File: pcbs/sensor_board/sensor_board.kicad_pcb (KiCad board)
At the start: 2 copper layers, 32 x 51 mm, 45 parts, among them J1 1.5mm, J2 2.5mm, J3 2.5mm, J4 1.5 mm, J5 RJ45, J6 Conn_01x06, Q1 220mA / 50V, Q2 220mA / 50V, Q3 220mA / 50V, U1 8-28V in / 5V 5W out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

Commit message: sensor board version 1.1
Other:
- board text added: "Brains"
- board text added: "J1"
- board text added: "J4"
- board text added: "Power"

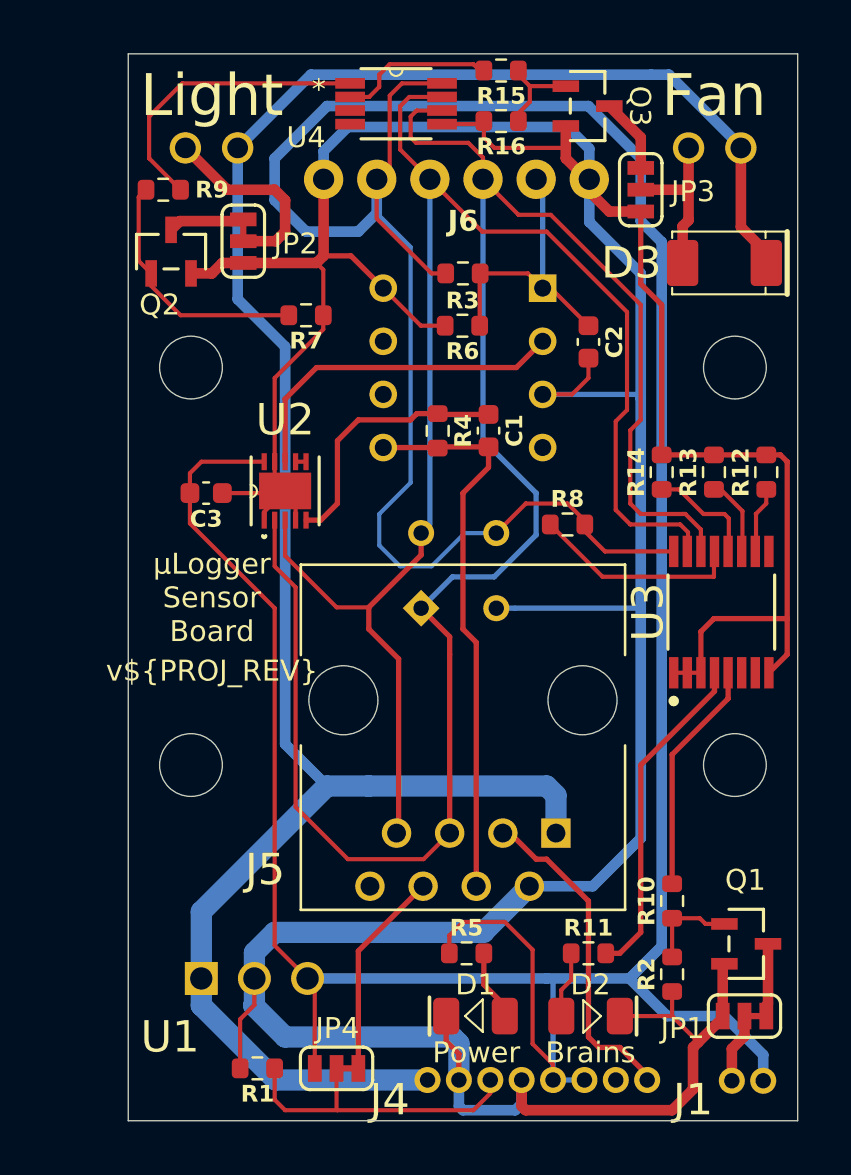
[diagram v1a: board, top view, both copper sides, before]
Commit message: upgrade to version 1.2
 - lower resistor for indicator LEDs (brighter)
 - better position for indicator LEDs (left/right)
 - io expander beam/indicator LED switched (=backwards compatibility)
 - switch contacts for the fan (opposite to the lights)
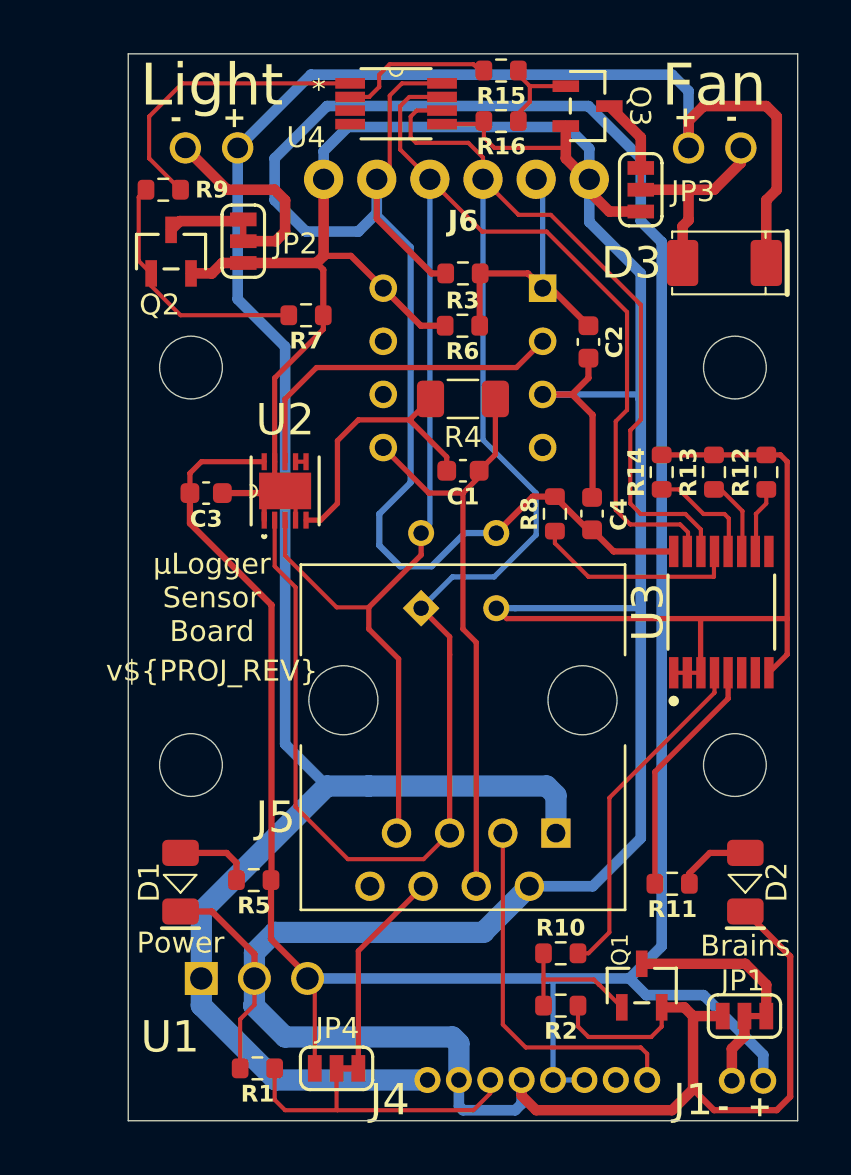
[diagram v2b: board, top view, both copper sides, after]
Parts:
- added C4: 100nF, footprints:C_0603, F.Cu at (154.7, 101.5)
- R11, R5: value 10kΩ -> 1kΩ
- R4: footprint footprints:R_0603 -> footprints:R_1206
- moved D1 15.5 mm to (135.0, 119.1), turned to 90 degrees
- moved R5 10.8 mm to (138.5, 119.0), turned to 180 degrees
- moved D2 9.78 mm to (162.0, 119.1), turned to 90 degrees
- moved R10 5.88 mm to (153.2, 122.5), turned to 0 degrees
- moved R2 5.53 mm to (153.2, 125.0), turned to 180 degrees
- moved Q1 5.38 mm to (157.0, 124.0), turned to 0 degrees
- moved R11 5.20 mm to (158.5, 119.2), turned to 180 degrees
- moved C1 2.27 mm to (148.5, 99.4), turned to 180 degrees
- moved R4 1.95 mm to (148.5, 96.0), turned to 180 degrees
- moved R8 0.79 mm to (152.9, 101.5), turned to 90 degrees
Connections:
- C1 pad 1: Net-(U2-P1B) -> /SIGNAL
- C1 pad 2: /SIGNAL -> Net-(U2-P1B)
- J3 pad 1: Net-(D3-A) -> +24V
- J3 pad 2: +24V -> Net-(D3-A)
- R10 pad 2: /LED -> /BEAM
- R11 pad 2: Net-(U3-P0) -> Net-(U3-P1)
- R4 pad 1: Net-(U2-P1B) -> /SIGNAL
- R4 pad 2: /SIGNAL -> Net-(U2-P1B)
- U3 pad 4: Net-(U3-P0) -> /BEAM
- U3 pad 5: /LED -> Net-(U3-P1)
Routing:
- net GND: track 223.4 -> 244.1 mm
- net /BEAM: track 0.00 -> 16.4 mm
- net Net-(U3-P0): track 16.0 -> 0.00 mm
- net +5V: track 194.9 -> 182.6 mm
- net Net-(U3-P1): track 0.00 -> 11.5 mm
- net /LED: track 11.2 -> 0.00 mm
- net +24V: track 103.0 -> 110.1 mm
- net Net-(JP1-A): track 3.49 -> 7.98 mm
- net Net-(Q1-G): track 4.46 -> 6.80 mm
- net /DECO: track 15.7 -> 17.9 mm
- net /SIGNAL: track 27.0 -> 29.0 mm
- net Net-(D3-A): track 7.75 -> 9.21 mm
- net Net-(U2-P1B): track 12.6 -> 13.3 mm
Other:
- board text added: "+"
- board text added: "-"

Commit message: sensor board version 1.3
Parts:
- removed the U2 at (140.0, 100.4)
- added J7: Conn_01x02, footprints:PIN_HEADERS_1X02, F.Cu at (155.0, 98.3)
- added J8: Conn_01x02, footprints:PIN_HEADERS_1X02, F.Cu at (146.2, 124.6)
- added U4: 100 kOhm, footprints:SOT-363_TSSOP6_SC88, F.Cu at (139.8, 100.2)
- added U5: 100 kOhm, footprints:SOT-363_TSSOP6_SC88, F.Cu at (136.3, 100.2)
- R4: value 27kΩ -> 10kΩ
- moved C3 2.74 mm to (133.5, 100.2), turned to 90 degrees
- moved R7 1.72 mm to (140.5, 90.4), turned to -90 degrees
- moved C2 1.58 mm to (155.0, 91.8)
- moved R3 0.50 mm to (148.5, 89.5)
- moved R6 0.50 mm to (148.5, 92.0)
- renumbered U3 to U2, U4 to U3
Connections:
- S1 pad 2: /IN- -> /AMP
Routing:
- net /SDA: track 72.3 -> 96.6 mm
- net /AMP: track 0.00 -> 24.1 mm
- net GND: track 244.1 -> 262.7 mm, vias 0 -> 2
- net /IN-: track 16.5 -> 0.00 mm
- net +5V: track 182.6 -> 169.6 mm, vias 0 -> 2
- net /SIGNAL: track 29.0 -> 41.7 mm
- net Net-(U4-W): track 0.00 -> 6.02 mm
- net /SCL: track 91.5 -> 97.4 mm
- net +24V: track 110.1 -> 113.6 mm
- net Net-(U2-P0W): track 0.50 -> 0.00 mm

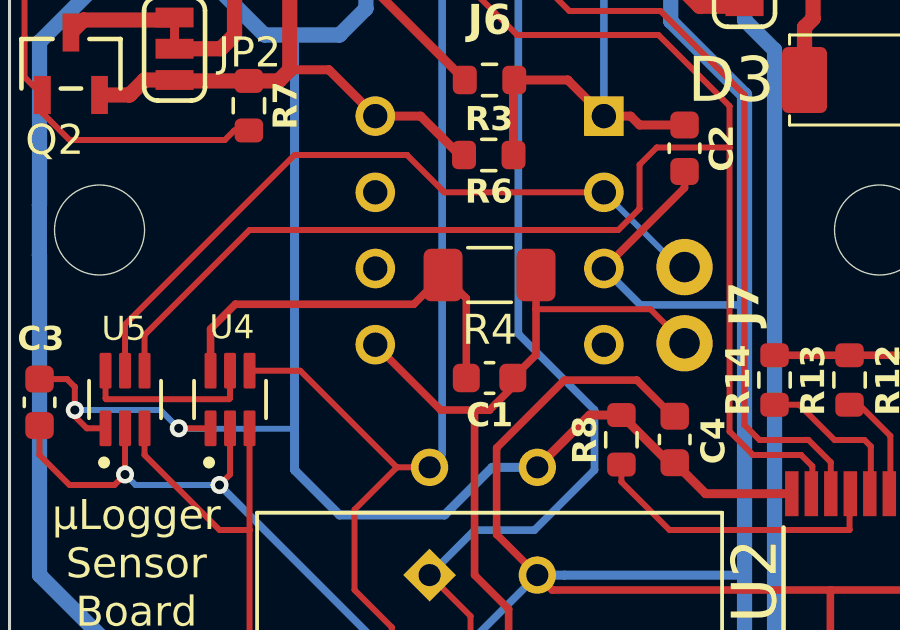
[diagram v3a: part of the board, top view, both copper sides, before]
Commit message: fix capacitor placaement on sensor board (IN- to SIGNAL)
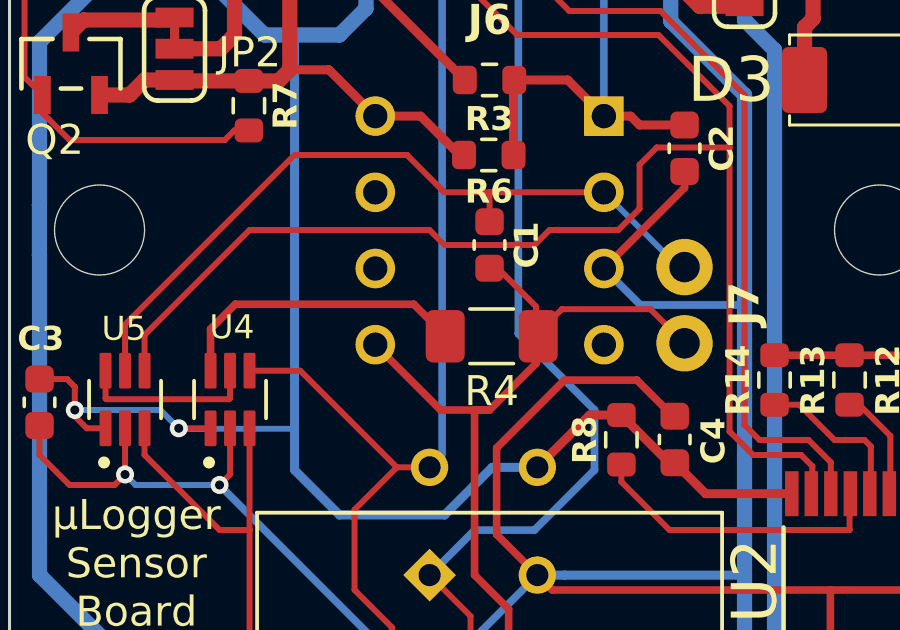
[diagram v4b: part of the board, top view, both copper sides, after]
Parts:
- moved C1 4.43 mm to (148.5, 95.0), turned to -90 degrees
- moved R4 2.04 mm to (148.6, 98.0)
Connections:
- C1 pad 1: /SIGNAL -> /AMP
- C1 pad 2: Net-(U4-B) -> /SIGNAL
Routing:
- net Net-(U4-B): track 13.6 -> 9.94 mm
- net /SIGNAL: track 41.7 -> 43.1 mm
- net /AMP: track 24.1 -> 25.1 mm
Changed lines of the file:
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@@
 	)
 	(property "PROJ_AUTHOR" "Sebastian Kopf")
-	(property "PROJ_REV" "1.3")
+	(property "PROJ_REV" "1.4")
 	(property "PROJ_TITLE" "µLogger Sensor Board")
 	(net 0 "")
@@
 	(footprint "footprints:C_0603"
 		(layer "F.Cu")
-		(at 148.500824 99.433241 180)
+		(at 148.5 95 -90)
 		(tags "SparkFun capacitor")
 		(property "Reference" "C1"
-			(at 0 -1.238192 0)
+			(at 0 -1.238192 90)
 			(layer "F.SilkS")
 			(effects
@@
 		)
 		(property "Value" "47pF"
-			(at 0 0 0)
+			(at 0 0 90)
 			(layer "Cmts.User")
 			(effects
@@
 		)
 		(property "Datasheet" "~"
-			(at 0 0 180)
+			(at 0 0 270)
 			(unlocked yes)
 			(layer "F.Fab")
@@
 		)
 		(property "Description" "Unpolarized capacitor"
-			(at 0 0 180)
+			(at 0 0 270)
 			(unlocked yes)
 			(layer "F.Fab")
@@
 		)
 		(property "JLCPCB" "C1671"
-			(at 0 0 180)
+			(at 0 0 270)
 			(unlocked yes)
 			(layer "F.Fab")
@@
 		)
 		(property "JLCPCBURL" "https://jlcpcb.com/partdetail/2023-CL10C470JB8NNNC/C1671"
-			(at 0 0 180)
+			(at 0 0 270)
 			(unlocked yes)
 			(layer "F.Fab")
@@
 		)
 		(fp_line
-			(start 1.48 0.73)
-			(end -1.48 0.73)
+			(start -1.48 0.73)
+			(end -1.48 -0.73)
 			(stroke
 				(width 0.05)
@@
 		)
 		(fp_line
-			(start 1.48 -0.73)
-			(end 1.48 0.73)
+			(start 1.48 0.73)
+			(end -1.48 0.73)
 			(stroke
 				(width 0.05)
@@
 		)
 		(fp_line
-			(start -1.48 0.73)
-			(end -1.48 -0.73)
+			(start -1.48 -0.73)
+			(end 1.48 -0.73)
 			(stroke
 				(width 0.05)
@@
 		)
 		(fp_line
-			(start -1.48 -0.73)
-			(end 1.48 -0.73)
+			(start 1.48 -0.73)
+			(end 1.48 0.73)
 			(stroke
 				(width 0.05)
@@
 		)
 		(fp_line
-			(start 0.8 0.4)
-			(end -0.8 0.4)
+			(start -0.8 0.4)
+			(end -0.8 -0.4)
 			(stroke
 				(width 0.1)
@@
 		)
 		(fp_line
-			(start 0.8 -0.4)
-			(end 0.8 0.4)
+			(start 0.8 0.4)
+			(end -0.8 0.4)
 			(stroke
 				(width 0.1)
@@
 		)
 		(fp_line
-			(start -0.8 0.4)
-			(end -0.8 -0.4)
+			(start -0.8 -0.4)
+			(end 0.8 -0.4)
 			(stroke
 				(width 0.1)
@@
 		)
 		(fp_line
-			(start -0.8 -0.4)
-			(end 0.8 -0.4)
+			(start 0.8 -0.4)
+			(end 0.8 0.4)
 			(stroke
 				(width 0.1)
@@
 		)
 		(pad "1" smd roundrect
-			(at -0.775 0 180)
+			(at -0.775 0 270)
 			(size 0.9 0.95)
 			(layers "F.Cu" "F.Mask" "F.Paste")
 			(roundrect_rratio 0.25)
-			(net 2 "/SIGNAL")
+			(net 30 "/AMP")
 			(pintype "passive")
 		)
 		(pad "2" smd roundrect
-			(at 0.775 0 180)
+			(at 0.775 0 270)
 			(size 0.9 0.95)
 			(layers "F.Cu" "F.Mask" "F.Paste")
 			(roundrect_rratio 0.25)
-			(net 25 "Net-(U4-B)")
+			(net 2 "/SIGNAL")
 			(pintype "passive")
 		)
@@
 	(footprint "footprints:R_1206"
 		(layer "F.Cu")
-		(at 148.5 96 180)
+		(at 148.571724 98.043223 180)
 		(descr "Resistor SMD 1206 (3216 Metric), square (rectangular) end terminal, IPC-7351 nominal with elongated pad for handsoldering")
 		(tags "resistor handsolder")
@@
 	)
 	(segment
-		(start 150.05 98.659064)
-		(end 150.05 97.140206)
-		(width 0.254)
-		(layer "F.Cu")
-		(net 2)
-	)
-	(segment
 		(start 148 106)
 		(end 149.1361 107.1361)
@@
 	)
 	(segment
-		(start 149.275824 99.433241)
-		(end 150.05 98.659064)
-		(width 0.254)
-		(layer "F.Cu")
-		(net 2)
-	)
-	(segment
 		(start 149.1361 119.2936)
 		(end 149.2311 119.3886)
@@
 	)
 	(segment
-		(start 150.05 97.140206)
-		(end 150.05 96)
-		(width 0.254)
+		(start 148.5 95.775)
+		(end 148.775 95.775)
+		(width 0.2)
 		(layer "F.Cu")
 		(net 2)
 	)
 	(segment
-		(start 149.275824 99.724176)
-		(end 149.275824 99.433241)
-		(width 0.254)
+		(start 150.05 97.05)
+		(end 150.05 98)
+		(width 0.2)
 		(layer "F.Cu")
 		(net 2)
 	)
 	(segment
-		(start 148.5 100.5)
-		(end 149.275824 99.724176)
-		(width 0.254)
+		(start 153.863965 97.140206)
+		(end 150.909794 97.140206)
+		(width 0.2)
 		(layer "F.Cu")
 		(net 2)
@@
 	)
 	(segment
-		(start 153.863965 97.140206)
-		(end 150.05 97.140206)
+		(start 150.05 98.95)
+		(end 150.05 98)
+		(width 0.254)
+		(layer "F.Cu")
+		(net 2)
+	)
+	(segment
+		(start 150.909794 97.140206)
+		(end 150.05 98)
+		(width 0.2)
+		(layer "F.Cu")
+		(net 2)
+	)
+	(segment
+		(start 148.775 95.775)
+		(end 150.05 97.05)
 		(width 0.2)
 		(layer "F.Cu")
@@
 	)
 	(segment
+		(start 148.5 100.5)
+		(end 150.05 98.95)
+		(width 0.254)
+		(layer "F.Cu")
+		(net 2)
+	)
+	(segment
 		(start 146.8675 100.5)
 		(end 144.6911 98.3236)
@@
 	)
 	(segment
+		(start 154.07505 91.74983)
+		(end 156.5 91.74983)
+		(width 0.2)
+		(layer "F.Cu")
+		(net 14)
+	)
+	(segment
 		(start 145.93496 81.56504)
 		(end 145.5 82)
@@
 	)
 	(segment
+		(start 152.792123 94.5)
+		(end 153.5 93.792123)
+		(width 0.2)
+		(layer "F.Cu")
+		(net 14)
+	)
+	(segment
 		(start 144 103.822996)
 		(end 145.411498 102.411498)
@@
 	)
 	(segment
-		(start 137 98)
-		(end 140.5 94.5)
+		(start 137 99.19)
+		(end 137 98)
 		(width 0.2)
 		(layer "F.Cu")
@@
 	(segment
 		(start 140.5 94.5)
-		(end 152.792123 94.5)
+		(end 146.5 94.5)
 		(width 0.2)
 		(layer "F.Cu")
@@
 	)
 	(segment
-		(start 152.792123 94.5)
-		(end 153.5 93.792123)
+		(start 153.5 93.792123)
+		(end 153.5 92.32488)
 		(width 0.2)
 		(layer "F.Cu")
@@
 	)
 	(segment
-		(start 153.5 93.792123)
-		(end 153.5 92.32488)
+		(start 156.5 90.367609)
+		(end 154.132391 88)
 		(width 0.2)
 		(layer "F.Cu")
@@
 	)
 	(segment
-		(start 153.5 92.32488)
-		(end 154.07505 91.74983)
+		(start 158.885683 102)
+		(end 157.285888 102)
 		(width 0.2)
 		(layer "F.Cu")
@@
 	)
 	(segment
-		(start 156.5 90.367609)
-		(end 154.132391 88)
+		(start 145.242776 107.742776)
+		(end 144 106.5)
 		(width 0.2)
 		(layer "F.Cu")
@@
 	)
 	(segment
-		(start 158.885683 102)
-		(end 157.285888 102)
+		(start 150 95)
+		(end 150.5 94.5)
 		(width 0.2)
 		(layer "F.Cu")
@@
 	)
 	(segment
-		(start 145.242776 107.742776)
-		(end 144 106.5)
+		(start 145.5 84.08)
+		(end 146.92 85.5)
 		(width 0.2)
 		(layer "F.Cu")
@@
 	)
 	(segment
-		(start 145.5 84.08)
-		(end 146.92 85.5)
+		(start 153.5 92.32488)
+		(end 154.07505 91.74983)
 		(width 0.2)
 		(layer "F.Cu")
@@
 	)
 	(segment
+		(start 150.5 94.5)
+		(end 152.792123 94.5)
+		(width 0.2)
+		(layer "F.Cu")
+		(net 14)
+	)
+	(segment
 		(start 142.19 99.19)
 		(end 140.5 99.19)
@@
 	)
 	(segment
-		(start 154.07505 91.74983)
-		(end 156.5 91.74983)
+		(start 159.260372 102.939006)
+		(end 159.260372 102.374689)
 		(width 0.2)
 		(layer "F.Cu")
@@
 	)
 	(segment
-		(start 159.260372 102.939006)
-		(end 159.260372 102.374689)
+		(start 146.5 94.5)
+		(end 147 95)
 		(width 0.2)
 		(layer "F.Cu")
@@
 	)
 	(segment
-		(start 137 99.19)
-		(end 137 98)
+		(start 147 95)
+		(end 150 95)
 		(width 0.2)
 		(layer "F.Cu")
@@
 	)
 	(segment
+		(start 137 98)
+		(end 140.5 94.5)
+		(width 0.2)
+		(layer "F.Cu")
+		(net 14)
+	)
+	(segment
 		(start 149.42 88)
 		(end 146.92 85.5)
@@
 	)
 	(segment
-		(start 147.725824 96.775824)
-		(end 147.725824 99.433241)
-		(width 0.254)
-		(layer "F.Cu")
-		(net 25)
-	)
-	(segment
-		(start 146.95 96)
-		(end 147.725824 96.775824)
-		(width 0.254)
+		(start 146.95 98)
+		(end 146.95 97.95)
+		(width 0.2)
 		(layer "F.Cu")
 		(net 25)
 	)
 	(segment
-		(start 145.975 96.975)
-		(end 146.95 96)
+		(start 140.025 96.975)
+		(end 139.2 97.8)
 		(width 0.254)
 		(layer "F.Cu")
@@
 	)
 	(segment
-		(start 140.025 96.975)
-		(end 139.2 97.8)
+		(start 146.95 97.95)
+		(end 145.975 96.975)
 		(width 0.254)
 		(layer "F.Cu")
@@
 	)
 	(segment
-		(start 146.9936 93.2436)
+		(start 148.5 93.2436)
 		(end 152.3111 93.2436)
 		(width 0.2)
@@
 	)
 	(segment
+		(start 148.5 94.225)
+		(end 148.5 93.2436)
+		(width 0.2)
+		(layer "F.Cu")
+		(net 30)
+	)
+	(segment
 		(start 142 92)
 		(end 145.75 92)
@@
 		(width 0.2)
 		(layer "F.Cu")
+		(net 30)
+	)
+	(segment
+		(start 146.9936 93.2436)
+		(end 148.5 93.2436)
+		(width 0.2)
+		(layer "F.Cu")

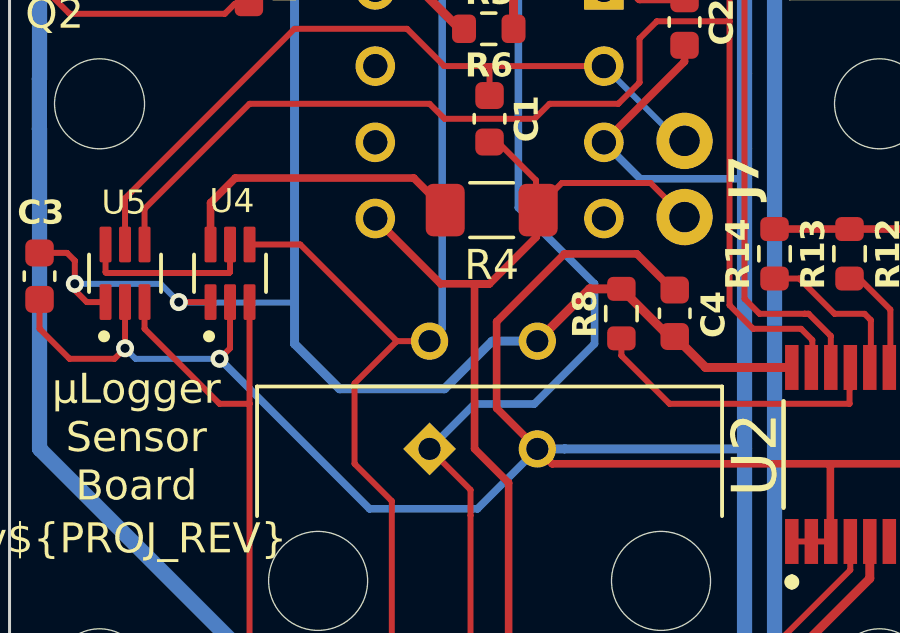
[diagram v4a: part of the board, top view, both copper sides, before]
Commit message: add signal stabilizing capacitors to controller and sensor boards
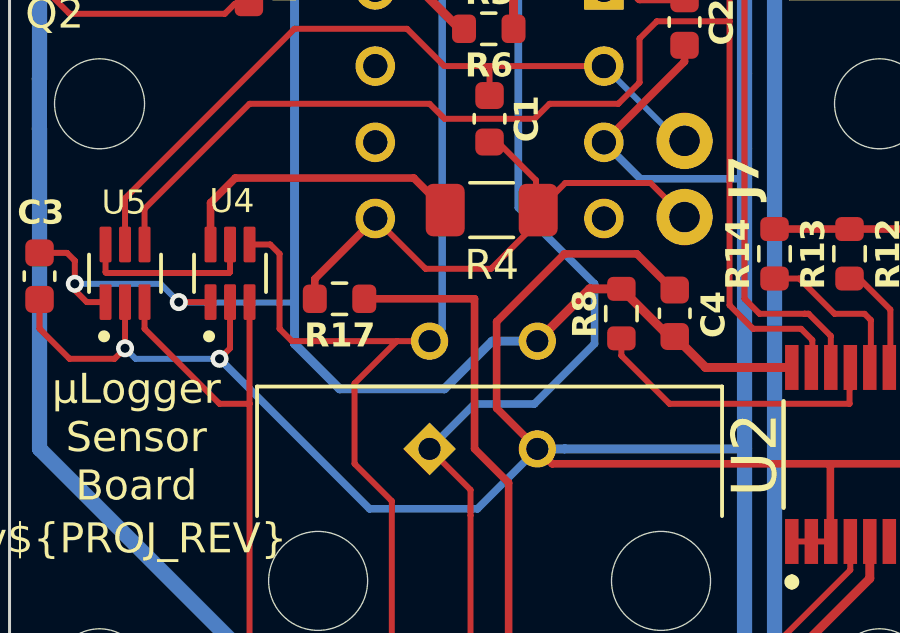
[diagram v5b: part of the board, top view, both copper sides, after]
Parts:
- added R17: 150Ω, footprints:R_0603, F.Cu at (143.5, 101.0)
- C1: value 47pF -> 100pF
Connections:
- C1 pad 2: /SIGNAL -> /OUTPUT
- J7 pad 1: /SIGNAL -> /OUTPUT
- R4 pad 1: /SIGNAL -> /OUTPUT
- S1 pad 5: /SIGNAL -> /OUTPUT
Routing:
- net /OUTPUT: track 0.00 -> 18.9 mm
- net /SIGNAL: track 43.1 -> 29.1 mm
- net /SDA: track 97.0 -> 98.5 mm

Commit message: sensor board version 1.4
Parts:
- removed R17: 150Ω, footprints:R_0603
- moved R10 1.00 mm to (153.2, 123.5)
- moved R2 1.00 mm to (153.2, 126.0)
- moved Q1 0.50 mm to (157.5, 124.1)
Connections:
- C1 pad 2: /OUTPUT -> /SIGNAL
- J7 pad 1: /OUTPUT -> /SIGNAL
- R4 pad 1: /OUTPUT -> /SIGNAL
- S1 pad 5: /OUTPUT -> /SIGNAL
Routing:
- net /OUTPUT: track 18.9 -> 0.00 mm
- net /SIGNAL: track 29.1 -> 42.7 mm
- net GND: track 262.7 -> 261.4 mm
- net /BEAM: track 16.4 -> 17.7 mm
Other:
- board text added: "GEOM.KOPFLAB.ORG"
